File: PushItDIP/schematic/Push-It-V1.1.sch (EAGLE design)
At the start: 30 parts, among them IC1 74LS595N, IC2 ATMEGA328P-PU, Q1 16MHZ

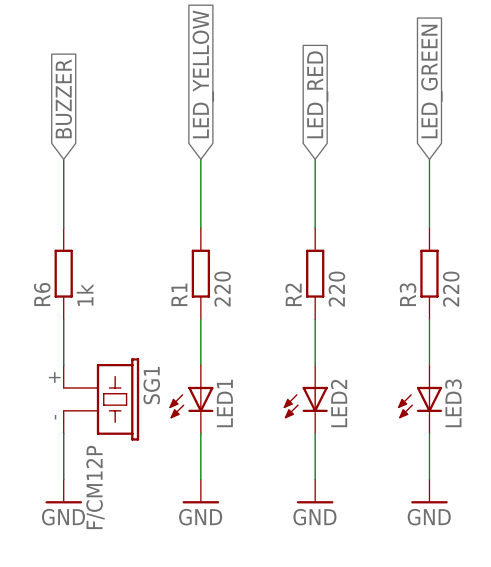
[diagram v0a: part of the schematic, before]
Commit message: PushItDIP: Finished documentation and adjusted resistor value
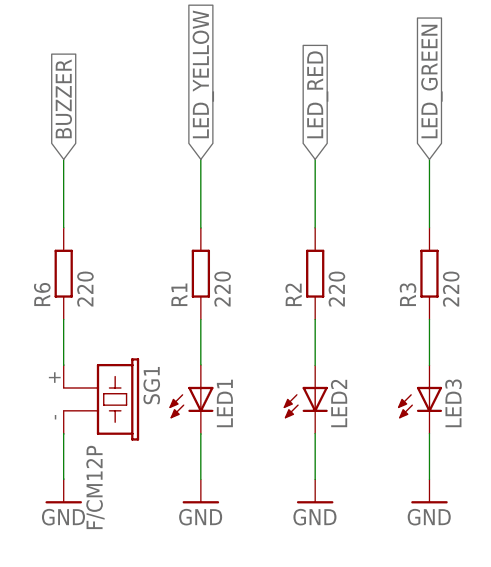
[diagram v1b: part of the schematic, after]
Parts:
- R6: value 1k -> 220
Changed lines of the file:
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@@
 <part name="R5" library="rcl" deviceset="R-EU_" device="0207/7" value="1k"/>
 <part name="GND7" library="supply1" deviceset="GND" device=""/>
-<part name="R6" library="rcl" deviceset="R-EU_" device="0207/7" value="1k"/>
+<part name="R6" library="rcl" deviceset="R-EU_" device="0207/7" value="220"/>
 <part name="ISP" library="avr-7" deviceset="AVR-ISP-6" device="VERT"/>
 <part name="IC2" library="avr-6" deviceset="MEGA48/88/168-PU" device="" value="ATMEGA328P-PU"/>
